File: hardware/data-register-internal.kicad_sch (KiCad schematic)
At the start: 4 parts, among them U8 74LV164A, U9 74LV164A

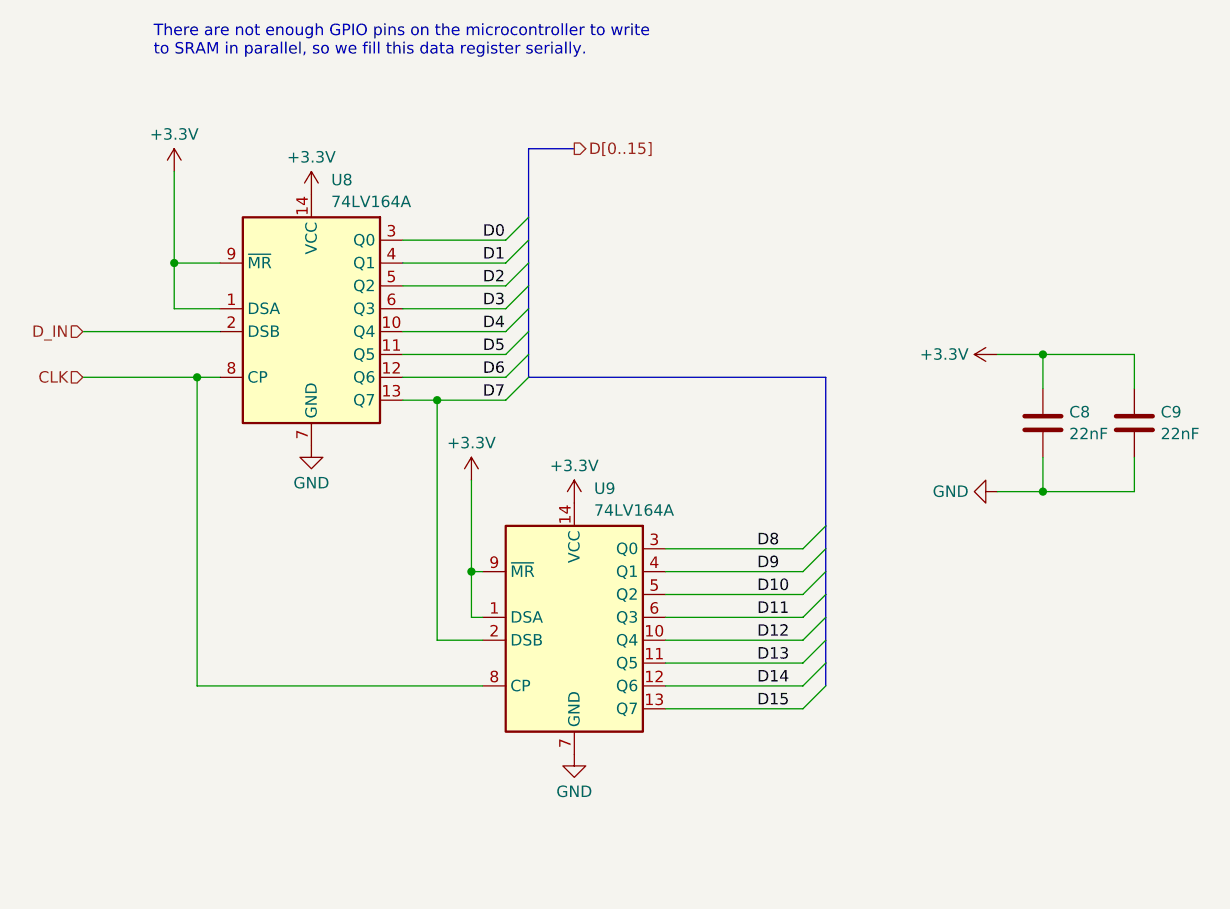
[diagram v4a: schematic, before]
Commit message: Move microcontroller board design into shareable subsheet
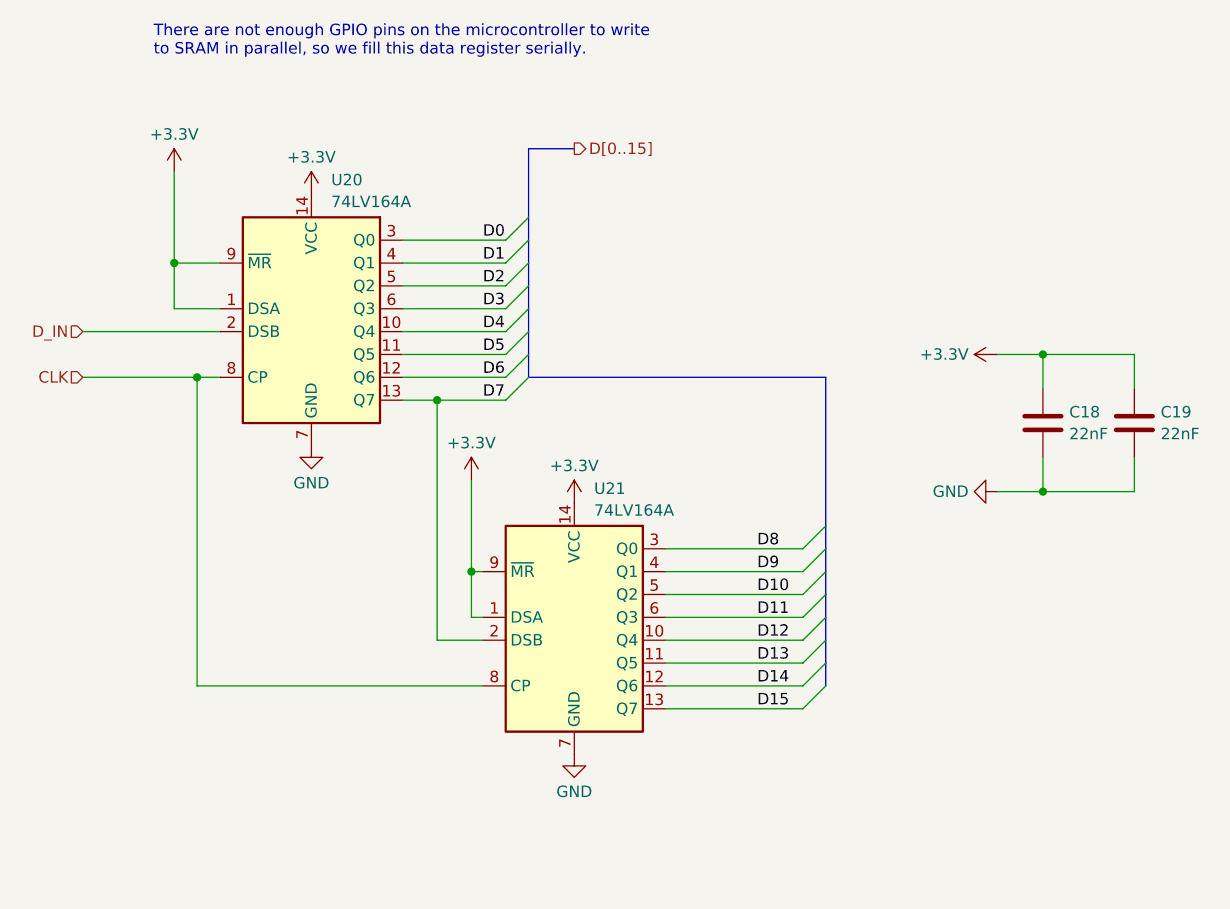
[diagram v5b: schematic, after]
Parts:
- renumbered C8 to C18, C9 to C19, U8 to U20, U9 to U21
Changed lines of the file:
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@@
 		(dnp no)
 		(fields_autoplaced yes)
-		(property "Reference" "C9"
+		(property "Reference" "C19"
 			(at 150.241 72.4478 0)
 			(effects
@@
 		(instances
 			(project "microcontroller"
-				(path "/eb0e957f-b2ea-4261-97c1-e28148a3f6e1/b911a2b2-03a3-4715-9f7c-39085d644f78"
-					(reference "C9")
+				(path "/eb0e957f-b2ea-4261-97c1-e28148a3f6e1/1f234c04-2a4a-4cc4-8cff-97e40dff5b3b/1764d238-7313-4b57-ab0a-5aa9beb7e234"
+					(reference "C19")
 					(unit 1)
 				)
@@
 		(dnp no)
 		(fields_autoplaced yes)
-		(property "Reference" "#PWR051"
+		(property "Reference" "#PWR079"
 			(at 85.09 86.36 0)
 			(effects
@@
 		(instances
 			(project "microcontroller"
-				(path "/eb0e957f-b2ea-4261-97c1-e28148a3f6e1/b911a2b2-03a3-4715-9f7c-39085d644f78"
-					(reference "#PWR051")
+				(path "/eb0e957f-b2ea-4261-97c1-e28148a3f6e1/1f234c04-2a4a-4cc4-8cff-97e40dff5b3b/1764d238-7313-4b57-ab0a-5aa9beb7e234"
+					(reference "#PWR079")
 					(unit 1)
 				)
@@
 		(dnp no)
 		(fields_autoplaced yes)
-		(property "Reference" "#PWR049"
+		(property "Reference" "#PWR078"
 			(at 73.66 83.82 0)
 			(effects
@@
 		(instances
 			(project "microcontroller"
-				(path "/eb0e957f-b2ea-4261-97c1-e28148a3f6e1/b911a2b2-03a3-4715-9f7c-39085d644f78"
-					(reference "#PWR049")
+				(path "/eb0e957f-b2ea-4261-97c1-e28148a3f6e1/1f234c04-2a4a-4cc4-8cff-97e40dff5b3b/1764d238-7313-4b57-ab0a-5aa9beb7e234"
+					(reference "#PWR078")
 					(unit 1)
 				)
@@
 		(dnp no)
 		(fields_autoplaced yes)
-		(property "Reference" "#PWR050"
+		(property "Reference" "#PWR075"
 			(at 40.64 49.53 0)
 			(effects
@@
 		(instances
 			(project "microcontroller"
-				(path "/eb0e957f-b2ea-4261-97c1-e28148a3f6e1/b911a2b2-03a3-4715-9f7c-39085d644f78"
-					(reference "#PWR050")
+				(path "/eb0e957f-b2ea-4261-97c1-e28148a3f6e1/1f234c04-2a4a-4cc4-8cff-97e40dff5b3b/1764d238-7313-4b57-ab0a-5aa9beb7e234"
+					(reference "#PWR075")
 					(unit 1)
 				)
@@
 		(dnp no)
 		(fields_autoplaced yes)
-		(property "Reference" "#PWR0118"
+		(property "Reference" "#PWR082"
 			(at 125.73 81.28 0)
 			(effects
@@
 		(instances
 			(project "microcontroller"
-				(path "/eb0e957f-b2ea-4261-97c1-e28148a3f6e1/b911a2b2-03a3-4715-9f7c-39085d644f78"
-					(reference "#PWR0118")
+				(path "/eb0e957f-b2ea-4261-97c1-e28148a3f6e1/1f234c04-2a4a-4cc4-8cff-97e40dff5b3b/1764d238-7313-4b57-ab0a-5aa9beb7e234"
+					(reference "#PWR082")
 					(unit 1)
 				)
@@
 		(dnp no)
 		(fields_autoplaced yes)
-		(property "Reference" "#PWR052"
+		(property "Reference" "#PWR081"
 			(at 135.89 66.04 0)
 			(effects
@@
 		(instances
 			(project "microcontroller"
-				(path "/eb0e957f-b2ea-4261-97c1-e28148a3f6e1/b911a2b2-03a3-4715-9f7c-39085d644f78"
-					(reference "#PWR052")
+				(path "/eb0e957f-b2ea-4261-97c1-e28148a3f6e1/1f234c04-2a4a-4cc4-8cff-97e40dff5b3b/1764d238-7313-4b57-ab0a-5aa9beb7e234"
+					(reference "#PWR081")
 					(unit 1)
 				)
@@
 		(dnp no)
 		(fields_autoplaced yes)
-		(property "Reference" "C8"
+		(property "Reference" "C18"
 			(at 140.081 72.4478 0)
 			(effects
@@
 		(instances
 			(project "microcontroller"
-				(path "/eb0e957f-b2ea-4261-97c1-e28148a3f6e1/b911a2b2-03a3-4715-9f7c-39085d644f78"
-					(reference "C8")
+				(path "/eb0e957f-b2ea-4261-97c1-e28148a3f6e1/1f234c04-2a4a-4cc4-8cff-97e40dff5b3b/1764d238-7313-4b57-ab0a-5aa9beb7e234"
+					(reference "C18")
 					(unit 1)
 				)
@@
 		(dnp no)
 		(fields_autoplaced yes)
-		(property "Reference" "#PWR053"
+		(property "Reference" "#PWR077"
 			(at 55.88 82.55 0)
 			(effects
@@
 		(instances
 			(project "microcontroller"
-				(path "/eb0e957f-b2ea-4261-97c1-e28148a3f6e1/b911a2b2-03a3-4715-9f7c-39085d644f78"
-					(reference "#PWR053")
+				(path "/eb0e957f-b2ea-4261-97c1-e28148a3f6e1/1f234c04-2a4a-4cc4-8cff-97e40dff5b3b/1764d238-7313-4b57-ab0a-5aa9beb7e234"
+					(reference "#PWR077")
 					(unit 1)
 				)
@@
 		(dnp no)
 		(fields_autoplaced yes)
-		(property "Reference" "#PWR048"
+		(property "Reference" "#PWR076"
 			(at 55.88 52.07 0)
 			(effects
@@
 		(instances
 			(project "microcontroller"
-				(path "/eb0e957f-b2ea-4261-97c1-e28148a3f6e1/b911a2b2-03a3-4715-9f7c-39085d644f78"
-					(reference "#PWR048")
+				(path "/eb0e957f-b2ea-4261-97c1-e28148a3f6e1/1f234c04-2a4a-4cc4-8cff-97e40dff5b3b/1764d238-7313-4b57-ab0a-5aa9beb7e234"
+					(reference "#PWR076")
 					(unit 1)
 				)
@@
 		(dnp no)
 		(fields_autoplaced yes)
-		(property "Reference" "#PWR054"
+		(property "Reference" "#PWR080"
 			(at 85.09 116.84 0)
 			(effects
@@
 		(instances
 			(project "microcontroller"
-				(path "/eb0e957f-b2ea-4261-97c1-e28148a3f6e1/b911a2b2-03a3-4715-9f7c-39085d644f78"
-					(reference "#PWR054")
+				(path "/eb0e957f-b2ea-4261-97c1-e28148a3f6e1/1f234c04-2a4a-4cc4-8cff-97e40dff5b3b/1764d238-7313-4b57-ab0a-5aa9beb7e234"
+					(reference "#PWR080")
 					(unit 1)
 				)
@@
 		(dnp no)
 		(fields_autoplaced yes)
-		(property "Reference" "U8"
+		(property "Reference" "U20"
 			(at 58.0741 46.6555 0)
 			(effects
@@
 		(instances
 			(project "microcontroller"
-				(path "/eb0e957f-b2ea-4261-97c1-e28148a3f6e1/b911a2b2-03a3-4715-9f7c-39085d644f78"
-					(reference "U8")
+				(path "/eb0e957f-b2ea-4261-97c1-e28148a3f6e1/1f234c04-2a4a-4cc4-8cff-97e40dff5b3b/1764d238-7313-4b57-ab0a-5aa9beb7e234"
+					(reference "U20")
 					(unit 1)
 				)
@@
 		(dnp no)
 		(fields_autoplaced yes)
-		(property "Reference" "U9"
+		(property "Reference" "U21"
 			(at 87.2841 80.9455 0)
 			(effects
@@
 		(instances
 			(project "microcontroller"
-				(path "/eb0e957f-b2ea-4261-97c1-e28148a3f6e1/b911a2b2-03a3-4715-9f7c-39085d644f78"
-					(reference "U9")
-					(unit 1)
-				)
+				(path "/eb0e957f-b2ea-4261-97c1-e28148a3f6e1/1f234c04-2a4a-4cc4-8cff-97e40dff5b3b/1764d238-7313-4b57-ab0a-5aa9beb7e234"
+					(reference "U21")
+					(unit 1)
+				)

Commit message: Reannotate schematics and drop debug bridges
Parts are now numbered starting at 0 for cart, 100 for SRAM, 300 for
microcontroller.

Also, drop debug bridges that made routing more difficult and had the
same names across prototype boards.

Hopefully this will help avoid naming conflicts for the unified PCB.

Also, redo prototype PCB layouts.

Now that all the names have changed, update board layouts.
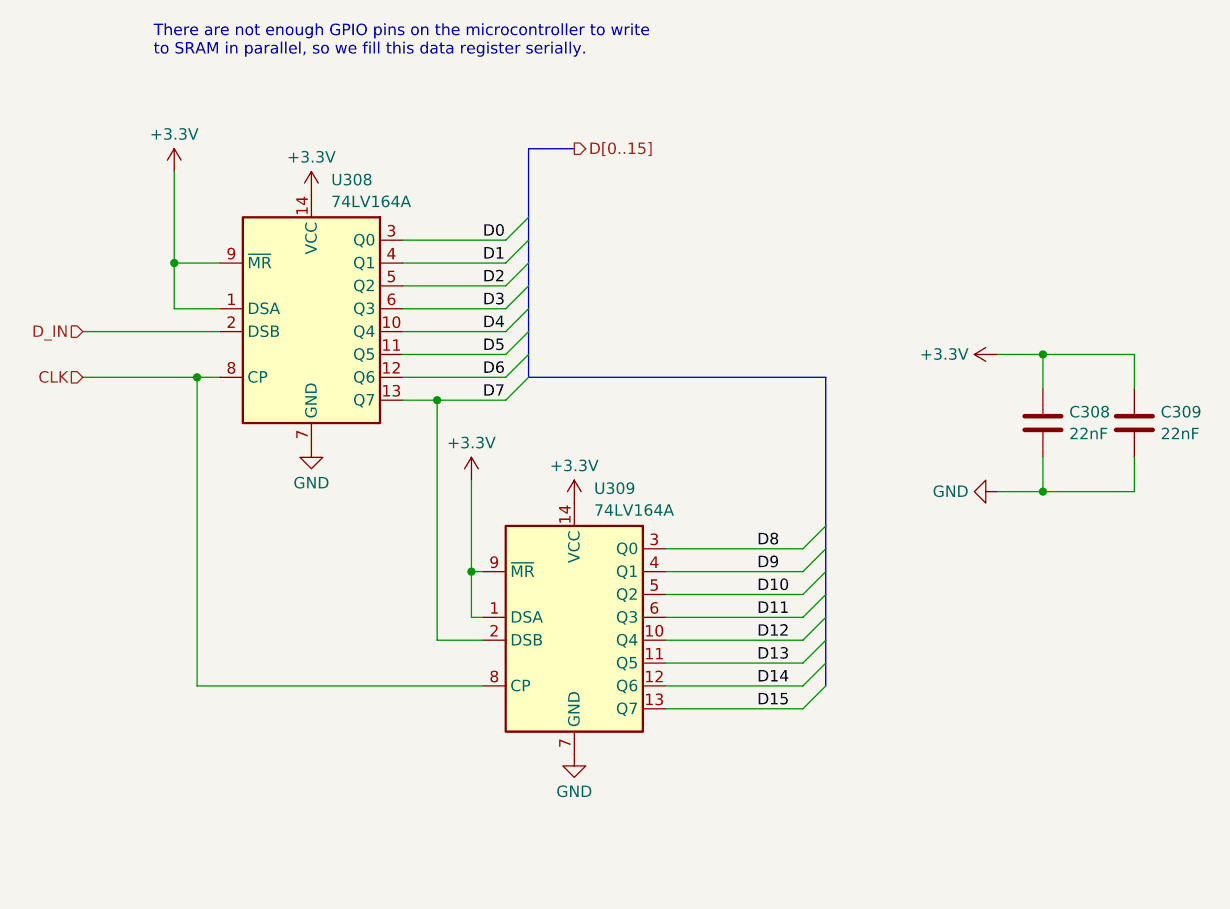
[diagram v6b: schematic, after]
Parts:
- renumbered C18 to C308, C19 to C309, U20 to U308, U21 to U309
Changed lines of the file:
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@@
 		(dnp no)
 		(fields_autoplaced yes)
-		(property "Reference" "C19"
+		(property "Reference" "C309"
 			(at 150.241 72.4478 0)
 			(effects
@@
 		(instances
 			(project "microcontroller"
-				(path "/eb0e957f-b2ea-4261-97c1-e28148a3f6e1/1f234c04-2a4a-4cc4-8cff-97e40dff5b3b/1764d238-7313-4b57-ab0a-5aa9beb7e234"
-					(reference "C19")
+				(path "/686046a3-64dc-4761-a4ce-3e2fd65204d5/7e8ae288-5866-48d7-b597-b9928e48743f/1764d238-7313-4b57-ab0a-5aa9beb7e234"
+					(reference "C309")
+					(unit 1)
+				)
+			)
+			(project "microcontroller"
+				(path "/eb0e957f-b2ea-4261-97c1-e28148a3f6e1/1f234c04-2a4a-4cc4-8cff-97e40dff5b3b/1764d238-7313-4b57-ab0a-5aa9beb7e234"
+					(reference "C314")
 					(unit 1)
 				)
@@
 		(dnp no)
 		(fields_autoplaced yes)
-		(property "Reference" "#PWR079"
+		(property "Reference" "#PWR0379"
 			(at 85.09 86.36 0)
 			(effects
@@
 		(instances
 			(project "microcontroller"
-				(path "/eb0e957f-b2ea-4261-97c1-e28148a3f6e1/1f234c04-2a4a-4cc4-8cff-97e40dff5b3b/1764d238-7313-4b57-ab0a-5aa9beb7e234"
-					(reference "#PWR079")
+				(path "/686046a3-64dc-4761-a4ce-3e2fd65204d5/7e8ae288-5866-48d7-b597-b9928e48743f/1764d238-7313-4b57-ab0a-5aa9beb7e234"
+					(reference "#PWR0379")
+					(unit 1)
+				)
+			)
+			(project "microcontroller"
+				(path "/eb0e957f-b2ea-4261-97c1-e28148a3f6e1/1f234c04-2a4a-4cc4-8cff-97e40dff5b3b/1764d238-7313-4b57-ab0a-5aa9beb7e234"
+					(reference "#PWR0379")
 					(unit 1)
 				)
@@
 		(dnp no)
 		(fields_autoplaced yes)
-		(property "Reference" "#PWR078"
+		(property "Reference" "#PWR0378"
 			(at 73.66 83.82 0)
 			(effects
@@
 		(instances
 			(project "microcontroller"
-				(path "/eb0e957f-b2ea-4261-97c1-e28148a3f6e1/1f234c04-2a4a-4cc4-8cff-97e40dff5b3b/1764d238-7313-4b57-ab0a-5aa9beb7e234"
-					(reference "#PWR078")
+				(path "/686046a3-64dc-4761-a4ce-3e2fd65204d5/7e8ae288-5866-48d7-b597-b9928e48743f/1764d238-7313-4b57-ab0a-5aa9beb7e234"
+					(reference "#PWR0378")
+					(unit 1)
+				)
+			)
+			(project "microcontroller"
+				(path "/eb0e957f-b2ea-4261-97c1-e28148a3f6e1/1f234c04-2a4a-4cc4-8cff-97e40dff5b3b/1764d238-7313-4b57-ab0a-5aa9beb7e234"
+					(reference "#PWR0378")
 					(unit 1)
 				)
@@
 		(dnp no)
 		(fields_autoplaced yes)
-		(property "Reference" "#PWR075"
+		(property "Reference" "#PWR0375"
 			(at 40.64 49.53 0)
 			(effects
@@
 		(instances
 			(project "microcontroller"
-				(path "/eb0e957f-b2ea-4261-97c1-e28148a3f6e1/1f234c04-2a4a-4cc4-8cff-97e40dff5b3b/1764d238-7313-4b57-ab0a-5aa9beb7e234"
-					(reference "#PWR075")
+				(path "/686046a3-64dc-4761-a4ce-3e2fd65204d5/7e8ae288-5866-48d7-b597-b9928e48743f/1764d238-7313-4b57-ab0a-5aa9beb7e234"
+					(reference "#PWR0375")
+					(unit 1)
+				)
+			)
+			(project "microcontroller"
+				(path "/eb0e957f-b2ea-4261-97c1-e28148a3f6e1/1f234c04-2a4a-4cc4-8cff-97e40dff5b3b/1764d238-7313-4b57-ab0a-5aa9beb7e234"
+					(reference "#PWR0375")
 					(unit 1)
 				)
@@
 		(dnp no)
 		(fields_autoplaced yes)
-		(property "Reference" "#PWR082"
+		(property "Reference" "#PWR0382"
 			(at 125.73 81.28 0)
 			(effects
@@
 		(instances
 			(project "microcontroller"
-				(path "/eb0e957f-b2ea-4261-97c1-e28148a3f6e1/1f234c04-2a4a-4cc4-8cff-97e40dff5b3b/1764d238-7313-4b57-ab0a-5aa9beb7e234"
-					(reference "#PWR082")
+				(path "/686046a3-64dc-4761-a4ce-3e2fd65204d5/7e8ae288-5866-48d7-b597-b9928e48743f/1764d238-7313-4b57-ab0a-5aa9beb7e234"
+					(reference "#PWR0382")
+					(unit 1)
+				)
+			)
+			(project "microcontroller"
+				(path "/eb0e957f-b2ea-4261-97c1-e28148a3f6e1/1f234c04-2a4a-4cc4-8cff-97e40dff5b3b/1764d238-7313-4b57-ab0a-5aa9beb7e234"
+					(reference "#PWR0382")
 					(unit 1)
 				)
@@
 		(dnp no)
 		(fields_autoplaced yes)
-		(property "Reference" "#PWR081"
+		(property "Reference" "#PWR0381"
 			(at 135.89 66.04 0)
 			(effects
@@
 		(instances
 			(project "microcontroller"
-				(path "/eb0e957f-b2ea-4261-97c1-e28148a3f6e1/1f234c04-2a4a-4cc4-8cff-97e40dff5b3b/1764d238-7313-4b57-ab0a-5aa9beb7e234"
-					(reference "#PWR081")
+				(path "/686046a3-64dc-4761-a4ce-3e2fd65204d5/7e8ae288-5866-48d7-b597-b9928e48743f/1764d238-7313-4b57-ab0a-5aa9beb7e234"
+					(reference "#PWR0381")
+					(unit 1)
+				)
+			)
+			(project "microcontroller"
+				(path "/eb0e957f-b2ea-4261-97c1-e28148a3f6e1/1f234c04-2a4a-4cc4-8cff-97e40dff5b3b/1764d238-7313-4b57-ab0a-5aa9beb7e234"
+					(reference "#PWR0381")
 					(unit 1)
 				)
@@
 		(dnp no)
 		(fields_autoplaced yes)
-		(property "Reference" "C18"
+		(property "Reference" "C308"
 			(at 140.081 72.4478 0)
 			(effects
@@
 		(instances
 			(project "microcontroller"
-				(path "/eb0e957f-b2ea-4261-97c1-e28148a3f6e1/1f234c04-2a4a-4cc4-8cff-97e40dff5b3b/1764d238-7313-4b57-ab0a-5aa9beb7e234"
-					(reference "C18")
+				(path "/686046a3-64dc-4761-a4ce-3e2fd65204d5/7e8ae288-5866-48d7-b597-b9928e48743f/1764d238-7313-4b57-ab0a-5aa9beb7e234"
+					(reference "C308")
+					(unit 1)
+				)
+			)
+			(project "microcontroller"
+				(path "/eb0e957f-b2ea-4261-97c1-e28148a3f6e1/1f234c04-2a4a-4cc4-8cff-97e40dff5b3b/1764d238-7313-4b57-ab0a-5aa9beb7e234"
+					(reference "C313")
 					(unit 1)
 				)
@@
 		(dnp no)
 		(fields_autoplaced yes)
-		(property "Reference" "#PWR077"
+		(property "Reference" "#PWR0377"
 			(at 55.88 82.55 0)
 			(effects
@@
 		(instances
 			(project "microcontroller"
-				(path "/eb0e957f-b2ea-4261-97c1-e28148a3f6e1/1f234c04-2a4a-4cc4-8cff-97e40dff5b3b/1764d238-7313-4b57-ab0a-5aa9beb7e234"
-					(reference "#PWR077")
+				(path "/686046a3-64dc-4761-a4ce-3e2fd65204d5/7e8ae288-5866-48d7-b597-b9928e48743f/1764d238-7313-4b57-ab0a-5aa9beb7e234"
+					(reference "#PWR0377")
+					(unit 1)
+				)
+			)
+			(project "microcontroller"
+				(path "/eb0e957f-b2ea-4261-97c1-e28148a3f6e1/1f234c04-2a4a-4cc4-8cff-97e40dff5b3b/1764d238-7313-4b57-ab0a-5aa9beb7e234"
+					(reference "#PWR0377")
 					(unit 1)
 				)
@@
 		(dnp no)
 		(fields_autoplaced yes)
-		(property "Reference" "#PWR076"
+		(property "Reference" "#PWR0376"
 			(at 55.88 52.07 0)
 			(effects
@@
 		(instances
 			(project "microcontroller"
-				(path "/eb0e957f-b2ea-4261-97c1-e28148a3f6e1/1f234c04-2a4a-4cc4-8cff-97e40dff5b3b/1764d238-7313-4b57-ab0a-5aa9beb7e234"
-					(reference "#PWR076")
+				(path "/686046a3-64dc-4761-a4ce-3e2fd65204d5/7e8ae288-5866-48d7-b597-b9928e48743f/1764d238-7313-4b57-ab0a-5aa9beb7e234"
+					(reference "#PWR0376")
+					(unit 1)
+				)
+			)
+			(project "microcontroller"
+				(path "/eb0e957f-b2ea-4261-97c1-e28148a3f6e1/1f234c04-2a4a-4cc4-8cff-97e40dff5b3b/1764d238-7313-4b57-ab0a-5aa9beb7e234"
+					(reference "#PWR0376")
 					(unit 1)
 				)
@@
 		(dnp no)
 		(fields_autoplaced yes)
-		(property "Reference" "#PWR080"
+		(property "Reference" "#PWR0380"
 			(at 85.09 116.84 0)
 			(effects
@@
 		(instances
 			(project "microcontroller"
-				(path "/eb0e957f-b2ea-4261-97c1-e28148a3f6e1/1f234c04-2a4a-4cc4-8cff-97e40dff5b3b/1764d238-7313-4b57-ab0a-5aa9beb7e234"
-					(reference "#PWR080")
+				(path "/686046a3-64dc-4761-a4ce-3e2fd65204d5/7e8ae288-5866-48d7-b597-b9928e48743f/1764d238-7313-4b57-ab0a-5aa9beb7e234"
+					(reference "#PWR0380")
+					(unit 1)
+				)
+			)
+			(project "microcontroller"
+				(path "/eb0e957f-b2ea-4261-97c1-e28148a3f6e1/1f234c04-2a4a-4cc4-8cff-97e40dff5b3b/1764d238-7313-4b57-ab0a-5aa9beb7e234"
+					(reference "#PWR0380")
 					(unit 1)
 				)
@@
 		(dnp no)
 		(fields_autoplaced yes)
-		(property "Reference" "U20"
+		(property "Reference" "U308"
 			(at 58.0741 46.6555 0)
 			(effects
@@
 		(instances
 			(project "microcontroller"
-				(path "/eb0e957f-b2ea-4261-97c1-e28148a3f6e1/1f234c04-2a4a-4cc4-8cff-97e40dff5b3b/1764d238-7313-4b57-ab0a-5aa9beb7e234"
-					(reference "U20")
+				(path "/686046a3-64dc-4761-a4ce-3e2fd65204d5/7e8ae288-5866-48d7-b597-b9928e48743f/1764d238-7313-4b57-ab0a-5aa9beb7e234"
+					(reference "U308")
+					(unit 1)
+				)
+			)
+			(project "microcontroller"
+				(path "/eb0e957f-b2ea-4261-97c1-e28148a3f6e1/1f234c04-2a4a-4cc4-8cff-97e40dff5b3b/1764d238-7313-4b57-ab0a-5aa9beb7e234"
+					(reference "U313")
 					(unit 1)
 				)
@@
 		(dnp no)
 		(fields_autoplaced yes)
-		(property "Reference" "U21"
+		(property "Reference" "U309"
 			(at 87.2841 80.9455 0)
 			(effects
@@
 		(instances
 			(project "microcontroller"
-				(path "/eb0e957f-b2ea-4261-97c1-e28148a3f6e1/1f234c04-2a4a-4cc4-8cff-97e40dff5b3b/1764d238-7313-4b57-ab0a-5aa9beb7e234"
-					(reference "U21")
-					(unit 1)
-				)
+				(path "/686046a3-64dc-4761-a4ce-3e2fd65204d5/7e8ae288-5866-48d7-b597-b9928e48743f/1764d238-7313-4b57-ab0a-5aa9beb7e234"
+					(reference "U309")
+					(unit 1)
+				)
+			)
+			(project "microcontroller"
+				(path "/eb0e957f-b2ea-4261-97c1-e28148a3f6e1/1f234c04-2a4a-4cc4-8cff-97e40dff5b3b/1764d238-7313-4b57-ab0a-5aa9beb7e234"
+					(reference "U314")
+					(unit 1)
+				)
